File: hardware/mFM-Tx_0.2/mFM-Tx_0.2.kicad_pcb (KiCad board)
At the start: 2 copper layers, 38 x 29.8 mm, 23 parts, among them P1 Header_1x6, P2 Header_1x9, P3 Header_2x3, P4 Header_1x5, P5 Header_1x2, P6 Header_1x2, Q1 ATmega368P-AU, SW1 SPDT, U1 TC1015-2.8V

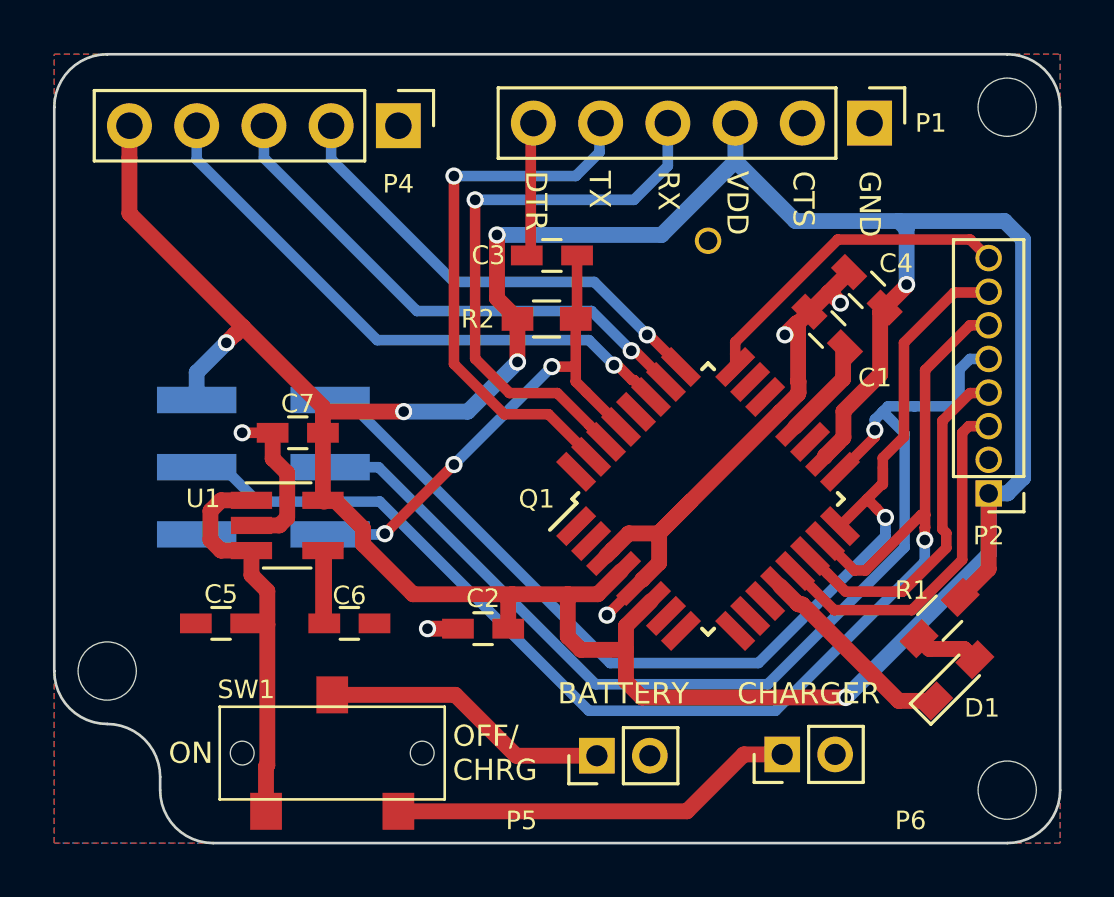
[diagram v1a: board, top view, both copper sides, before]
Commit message: Updated VDD to 3.3V on mFM-Tx_0.2
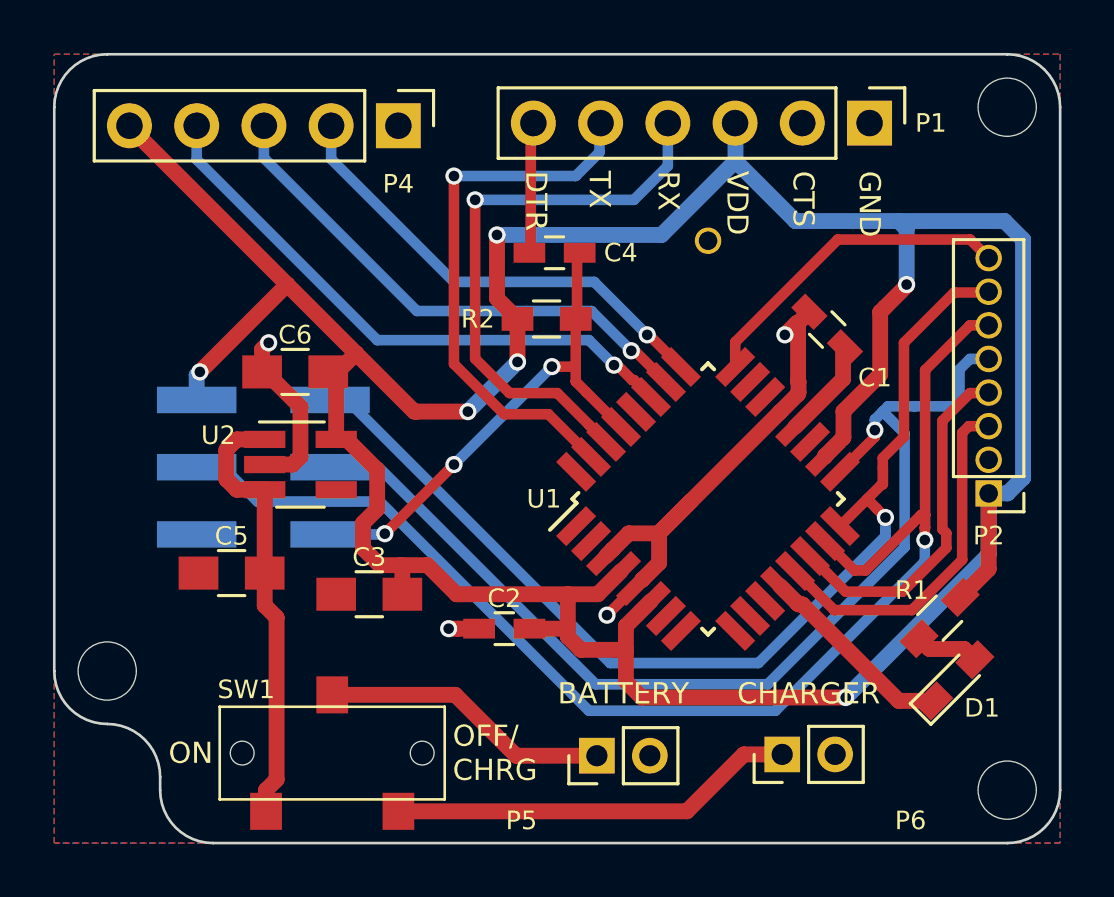
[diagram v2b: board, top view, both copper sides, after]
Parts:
- removed C7: 1uF, Capacitors_SMD:C_0603_HandSoldering
- removed Q1: ATmega368P-AU, Housings_QFP:TQFP-32_7x7mm_Pitch0.8mm
- added U2: MIC5205-3.3, TO_SOT_Packages_SMD:SOT-23-5_HandSoldering, F.Cu at (149.3, 111.2)
- C3: value 0.1uF -> 4.7uF; footprint Capacitors_SMD:C_0603_HandSoldering -> Capacitors_SMD:C_0805_HandSoldering
- C4: value 1uF -> 0.1uF
- C5: value 1uF -> 4.7uF; footprint Capacitors_SMD:C_0603_HandSoldering -> Capacitors_SMD:C_0805_HandSoldering
- C6: value 470pF -> 4.7uF; footprint Capacitors_SMD:C_0603_HandSoldering -> Capacitors_SMD:C_0805_HandSoldering
- U1: value TC1015-2.8V -> ATmega368P-AU; footprint TO_SOT_Packages_SMD:SOT-23-5_HandSoldering -> Housings_QFP:TQFP-32_7x7mm_Pitch0.8mm
- moved U1 15.9 mm to (164.7, 112.5), turned to 45 degrees
- moved C3 14.5 mm to (151.9, 116.1)
- moved C4 11.9 mm to (158.9, 103.2), turned to 180 degrees
- moved C6 9.72 mm to (149.1, 107.7), turned to 180 degrees
- moved C5 1.94 mm to (146.7, 115.3)
- moved C2 0.80 mm to (157.0, 117.4)
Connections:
- C3 pad 1: PROG_RST -> +VDD
- C3 pad 2: PROG_DTR -> GND
- C4 pad 1: +VDD -> PROG_RST
- C4 pad 2: GND -> PROG_DTR
- C6 pad 1: /LDO_BYP -> +VDD
- U1 pad 1: LDO_VBATT -> Net-(U1-Pad1)
- U1 pad 2: GND -> Net-(U1-Pad2)
- U1 pad 3: LDO_VBATT -> GND
- U1 pad 4: /LDO_BYP -> +VDD
- U1 pad 5: +VDD -> GND
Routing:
- net +VDD: track 123.6 -> 128.5 mm
- net /LDO_BYP: track 2.74 -> 0.00 mm
- net GND: track 29.0 -> 26.8 mm, vias 5 -> 4
- net LDO_VBATT: track 15.5 -> 16.8 mm
